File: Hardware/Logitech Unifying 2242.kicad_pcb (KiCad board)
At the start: 2 copper layers, 22 x 42 mm, 13 parts, among them J1 Bus_M.2_Socket_B, U1 TPS613222ADBV

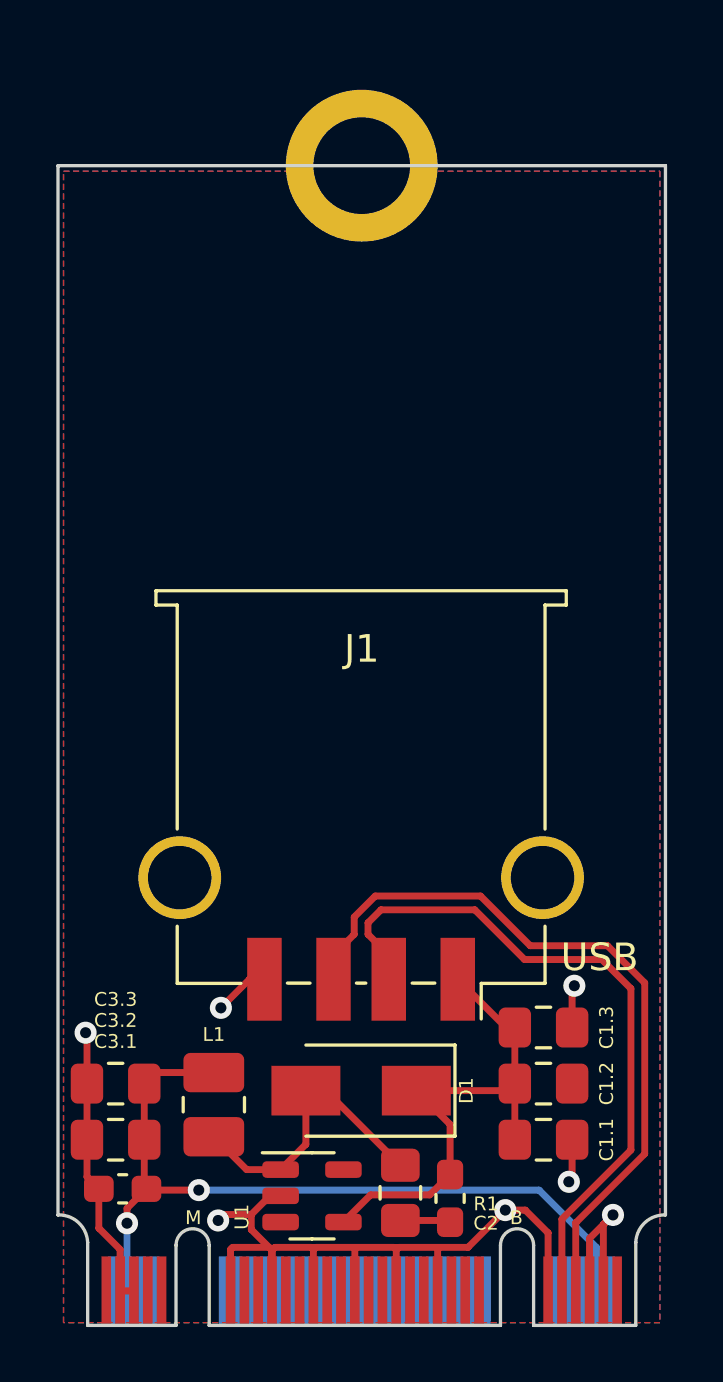
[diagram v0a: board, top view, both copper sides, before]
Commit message: Add cutout for low-clearance use
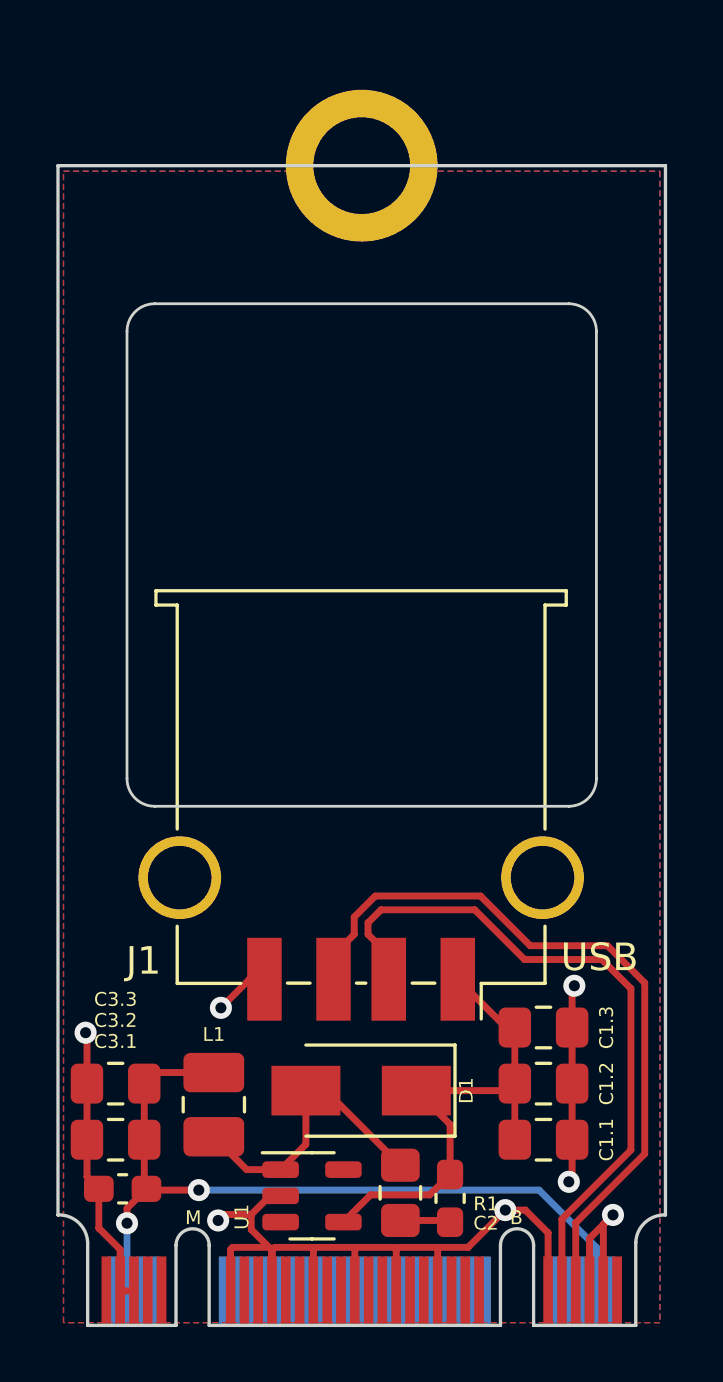
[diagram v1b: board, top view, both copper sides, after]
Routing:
- net GND: track 51.1 -> 55.1 mm

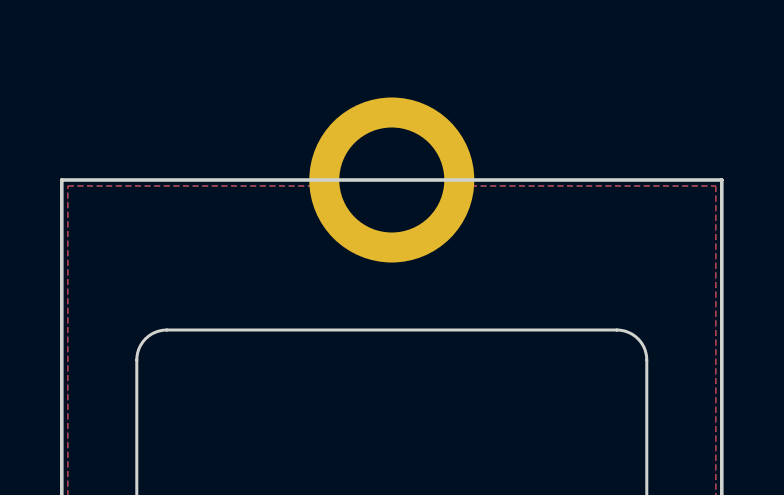
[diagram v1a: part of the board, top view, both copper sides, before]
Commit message: Change screw hole pad and PCB text
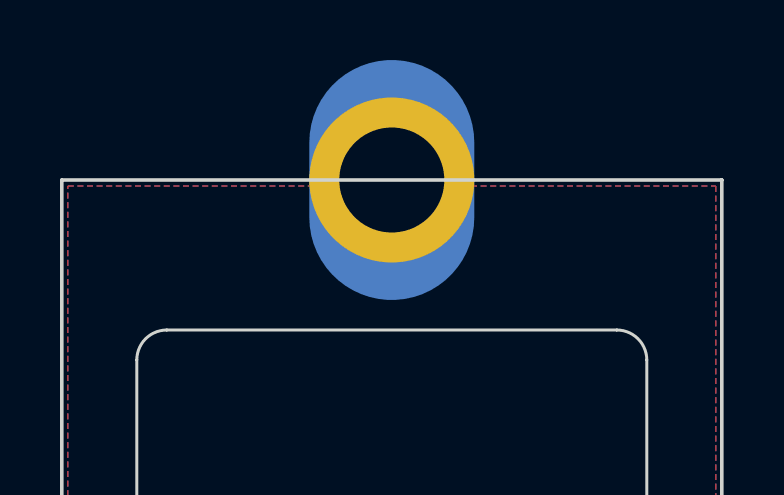
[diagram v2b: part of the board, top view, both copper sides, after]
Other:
- board text added: "${TITLE} Revision ${REVISION} ${COMMENT1} ${ISSUE_DATE}"
- board text removed: "${TITLE} Revision ${REVISION} ${ISSUE_DATE}"

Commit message: Update M.2 footprints
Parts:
- J1: footprint Connector_OTHER:M.2-2242-B+M-KEY -> Connector_OTHER:M.2-2242-B+M-KEY_USB-ONLY
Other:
- outline, holes or cut-outs redrawn

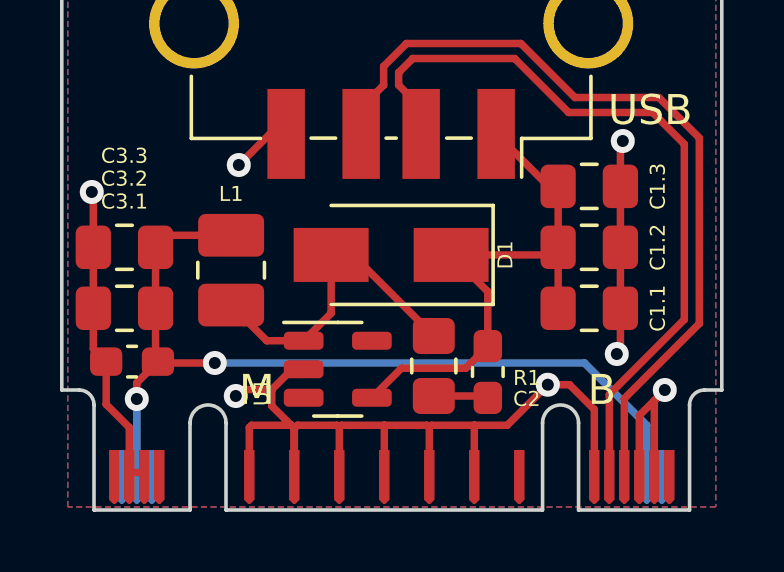
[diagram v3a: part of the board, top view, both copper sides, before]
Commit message: Update footprint and board settings (via size, pours, etc)
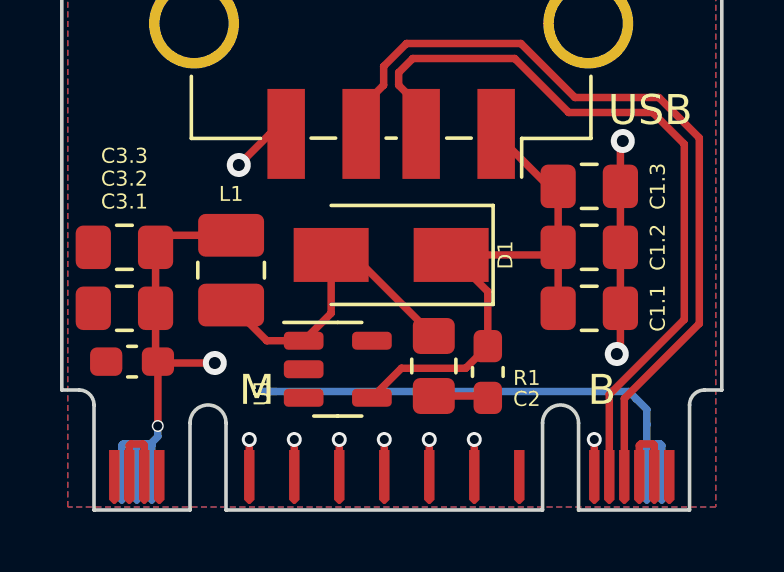
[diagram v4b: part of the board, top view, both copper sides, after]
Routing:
- net GND: track 55.1 -> 23.2 mm, vias 7 -> 10
- net +3V3: track 30.8 -> 33.4 mm

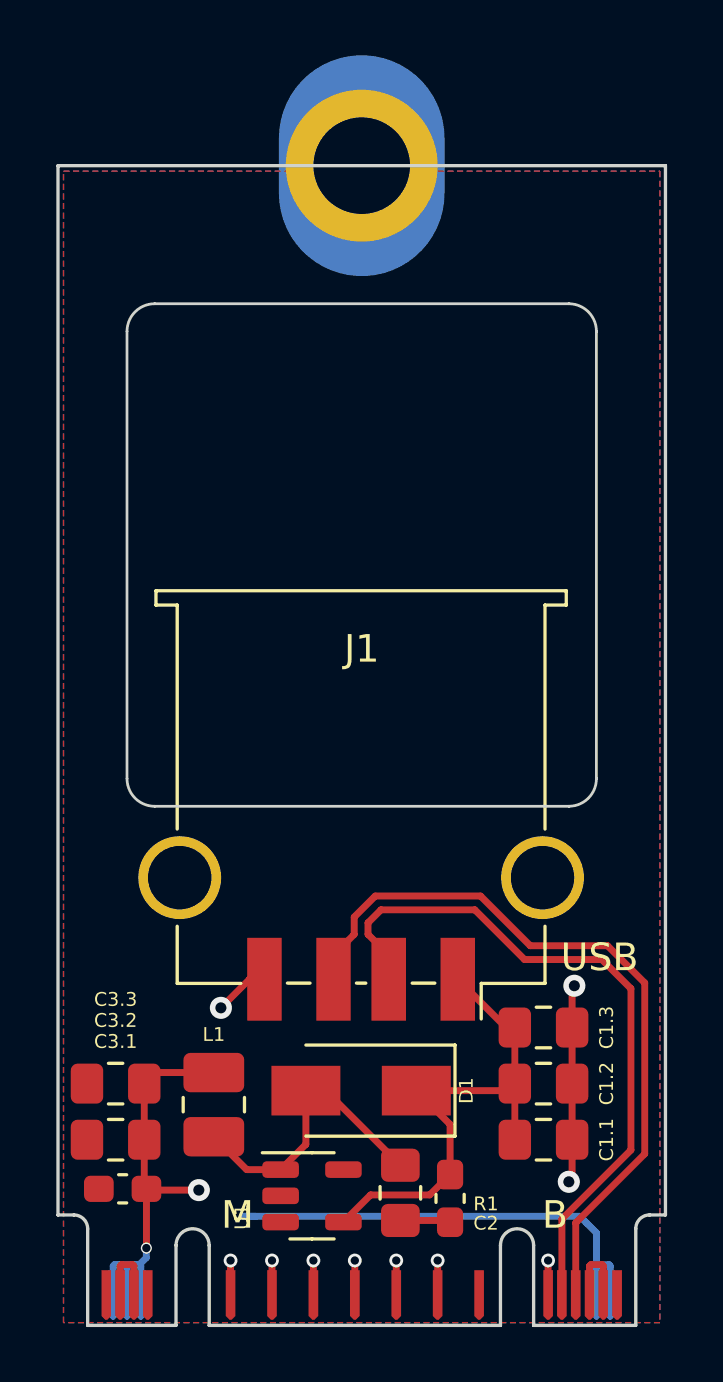
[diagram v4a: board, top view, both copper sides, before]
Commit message: Reroute after added fuse and new footprints
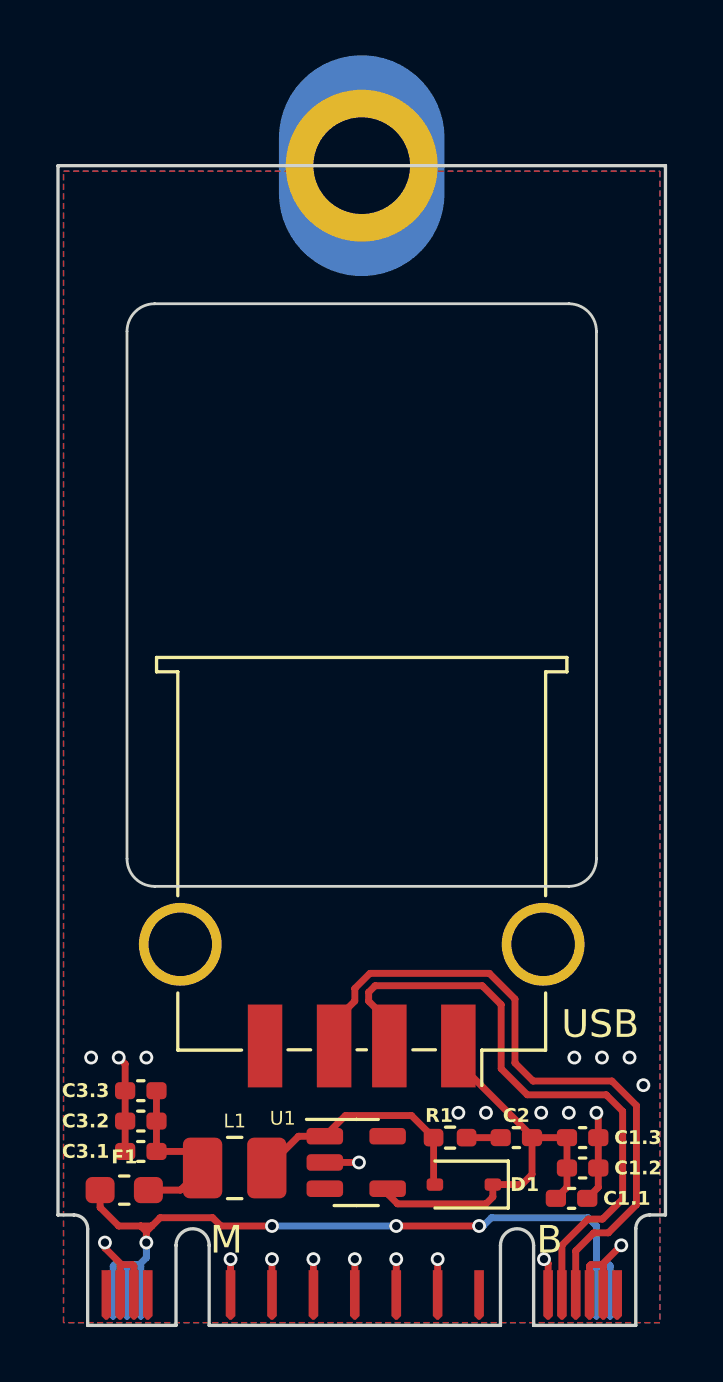
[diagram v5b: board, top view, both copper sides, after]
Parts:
- added F1: 1A, Fuse:Fuse_0603_1608Metric_Pad1.05x0.95mm_HandSolder, F.Cu at (130.0, 116.3)
- C1.1, C1.2, C1.3, C3.2, C3.3: footprint Capacitor_SMD:C_0805_2012Metric_Pad1.18x1.45mm_HandSolder -> Capacitor_SMD:C_0402_1005Metric_Pad0.74x0.62mm_HandSolder
- C2: value 150pF -> 1000pF; footprint Capacitor_SMD:C_0603_1608Metric_Pad1.08x0.95mm_HandSolder -> Capacitor_SMD:C_0402_1005Metric_Pad0.74x0.62mm_HandSolder
- C3.1: footprint Capacitor_SMD:C_0603_1608Metric_Pad1.08x0.95mm_HandSolder -> Capacitor_SMD:C_0402_1005Metric_Pad0.74x0.62mm_HandSolder
- D1: footprint Diode_SMD:D_SMA -> Diode_SMD:D_SOD-323
- R1: footprint Resistor_SMD:R_0805_2012Metric_Pad1.20x1.40mm_HandSolder -> Resistor_SMD:R_0402_1005Metric_Pad0.72x0.64mm_HandSolder
- moved D1 5.04 mm to (142.3, 116.1)
- moved C1.3 4.23 mm to (146.6, 114.4)
- moved C1.2 3.37 mm to (146.6, 115.5)
- moved C2 3.26 mm to (144.2, 114.4), turned to 0 degrees
- moved R1 2.69 mm to (141.8, 114.4), turned to 0 degrees
- moved USB 2.42 mm to (138.6, 104.7)
- moved L1 2.42 mm to (134.0, 115.5), turned to 0 degrees
- moved C1.1 2.36 mm to (146.2, 116.6)
- moved U1 2.00 mm to (138.4, 115.3)
- moved C3.1 1.51 mm to (130.6, 114.9)
- moved C3.2 1.14 mm to (130.6, 113.8)
- moved C3.3 0.95 mm to (130.6, 112.7)
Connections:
- C3.1 pad 1: +3V3 -> /3V3 PROT
- C3.2 pad 1: +3V3 -> /3V3 PROT
- C3.3 pad 1: +3V3 -> /3V3 PROT
- L1 pad 1: +3V3 -> /3V3 PROT
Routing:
- net /3V3 PROT: track 0.00 -> 6.41 mm
- net +3V3: track 33.4 -> 30.0 mm, vias 2 -> 4
- net +5V: track 18.6 -> 15.7 mm
- net Net-(D1-A): track 10.7 -> 8.88 mm
- net /USBD+: track 26.9 -> 25.1 mm
- net /USBD-: track 25.2 -> 23.5 mm
- net GND: track 23.2 -> 24.5 mm, vias 10 -> 22
- net Net-(C2-Pad1): track 1.83 -> 1.23 mm

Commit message: Add test points (#1) and other finishing touches
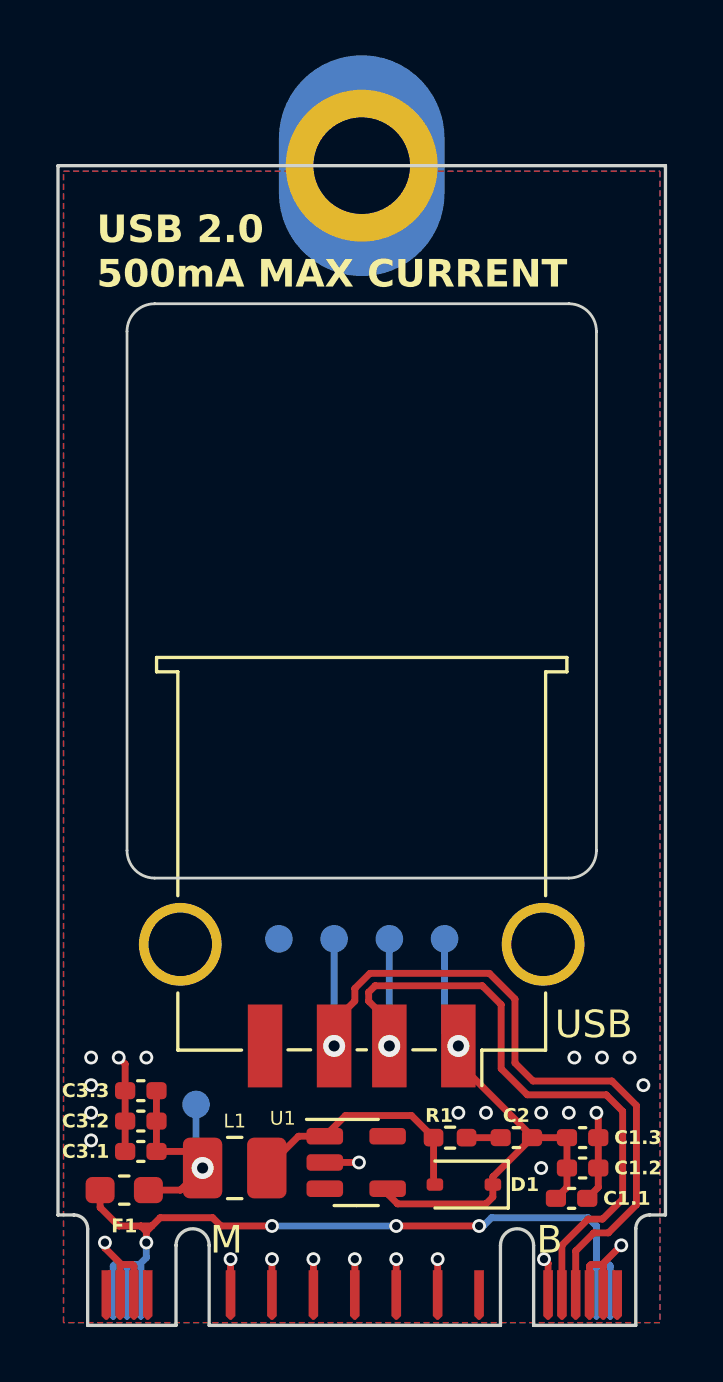
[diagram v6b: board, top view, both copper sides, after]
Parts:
- added TP1: GND, TestPoint:TestPoint_Pad_D1.0mm, B.Cu at (135.6, 107.2)
- added TP2: 3V3, TestPoint:TestPoint_Pad_D1.0mm, B.Cu at (132.6, 113.2)
- added TP3: 5V, TestPoint:TestPoint_Pad_D1.0mm, B.Cu at (141.6, 107.2)
- added TP4: D+, TestPoint:TestPoint_Pad_D1.0mm, B.Cu at (137.6, 107.2)
- added TP5: D-, TestPoint:TestPoint_Pad_D1.0mm, B.Cu at (139.6, 107.2)
- renumbered USB to J2
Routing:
- net /USBD-: track 23.5 -> 27.4 mm, vias 0 -> 1
- net /USBD+: track 25.1 -> 29.0 mm, vias 0 -> 1
- net +5V: track 15.7 -> 19.1 mm, vias 0 -> 1
- net /3V3 PROT: track 6.41 -> 8.81 mm, vias 0 -> 1
- net GND: vias 22 -> 26
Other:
- board text added: "USB 2.0 500mA MAX CURRENT"

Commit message: Add missing net names
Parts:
- F1: value 1A -> 500mA
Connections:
- net Net-(C2-Pad1) renamed /SNUBBER RC
- net Net-(D1-A) renamed /BOOST IN
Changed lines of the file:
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@@
   (net 1 "+5V")
   (net 2 "GND")
-  (net 3 "Net-(C2-Pad1)")
+  (net 3 "/SNUBBER RC")
   (net 4 "+3V3")
-  (net 5 "Net-(D1-A)")
+  (net 5 "/BOOST IN")
   (net 6 "/USBD+")
   (net 7 "/USBD-")
@@
       (stroke (width 0.1) (type solid)) (layer "F.Fab"))
     (pad "1" smd roundrect (at -1.1375 -0.95) (size 1.325 0.6) (layers "F.Cu" "F.Paste" "F.Mask") (roundrect_rratio 0.25)
-      (net 5 "Net-(D1-A)") (pinfunction "SW") (pintype "power_in"))
+      (net 5 "/BOOST IN") (pinfunction "SW") (pintype "power_in"))
     (pad "2" smd roundrect (at -1.1375 0) (size 1.325 0.6) (layers "F.Cu" "F.Paste" "F.Mask") (roundrect_rratio 0.25)
       (net 2 "GND") (pinfunction "GND") (pintype "power_in"))
@@
       (stroke (width 0.1) (type solid)) (layer "F.Fab"))
     (pad "1" smd roundrect (at -0.5675 0) (size 0.735 0.62) (layers "F.Cu" "F.Paste" "F.Mask") (roundrect_rratio 0.25)
-      (net 3 "Net-(C2-Pad1)") (pintype "passive"))
+      (net 3 "/SNUBBER RC") (pintype "passive"))
     (pad "2" smd roundrect (at 0.5675 0) (size 0.735 0.62) (layers "F.Cu" "F.Paste" "F.Mask") (roundrect_rratio 0.25)
       (net 1 "+5V") (pintype "passive"))
@@
         (effects (font (size 0.5 0.5) (thickness 0.1) bold))
     )
-    (fp_text value "1A" (at 0 1.43) (layer "F.Fab")
+    (fp_text value "500mA" (at 0 1.43) (layer "F.Fab")
         (effects (font (size 1 1) (thickness 0.15)))
     )
@@
       (net 14 "/3V3 PROT") (pinfunction "1") (pintype "passive"))
     (pad "2" smd roundrect (at 1.1625 0) (size 1.425 2.2) (layers "F.Cu" "F.Paste" "F.Mask") (roundrect_rratio 0.1754392982)
-      (net 5 "Net-(D1-A)") (pinfunction "2") (pintype "passive"))
+      (net 5 "/BOOST IN") (pinfunction "2") (pintype "passive"))
     (model "${KICAD6_3DMODEL_DIR}/Inductor_SMD.3dshapes/L_1008_2520Metric.wrl"
       (offset (xyz 0 0 0))
@@
       (net 1 "+5V") (pinfunction "K") (pintype "passive"))
     (pad "2" smd roundrect (at 1.05 0 180) (size 0.6 0.45) (layers "F.Cu" "F.Paste" "F.Mask") (roundrect_rratio 0.25)
-      (net 5 "Net-(D1-A)") (pinfunction "A") (pintype "passive"))
+      (net 5 "/BOOST IN") (pinfunction "A") (pintype "passive"))
     (model "${KICAD6_3DMODEL_DIR}/Diode_SMD.3dshapes/D_SOD-323.wrl"
       (offset (xyz 0 0 0))
@@
       (stroke (width 0.1) (type solid)) (layer "F.Fab"))
     (pad "1" smd roundrect (at -0.5975 0) (size 0.715 0.64) (layers "F.Cu" "F.Paste" "F.Mask") (roundrect_rratio 0.25)
-      (net 5 "Net-(D1-A)") (pintype "passive"))
+      (net 5 "/BOOST IN") (pintype "passive"))
     (pad "2" smd roundrect (at 0.5975 0) (size 0.715 0.64) (layers "F.Cu" "F.Paste" "F.Mask") (roundrect_rratio 0.25)
-      (net 3 "Net-(C2-Pad1)") (pintype "passive"))
+      (net 3 "/SNUBBER RC") (pintype "passive"))
     (model "${KICAD6_3DMODEL_DIR}/Resistor_SMD.3dshapes/R_0402_1005Metric.wrl"
       (offset (xyz 0 0 0))
